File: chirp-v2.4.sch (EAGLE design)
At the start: 19 parts, among them IC1 TINY24/44/84-SSU, SW1 SPST_TACTFSMJSMA

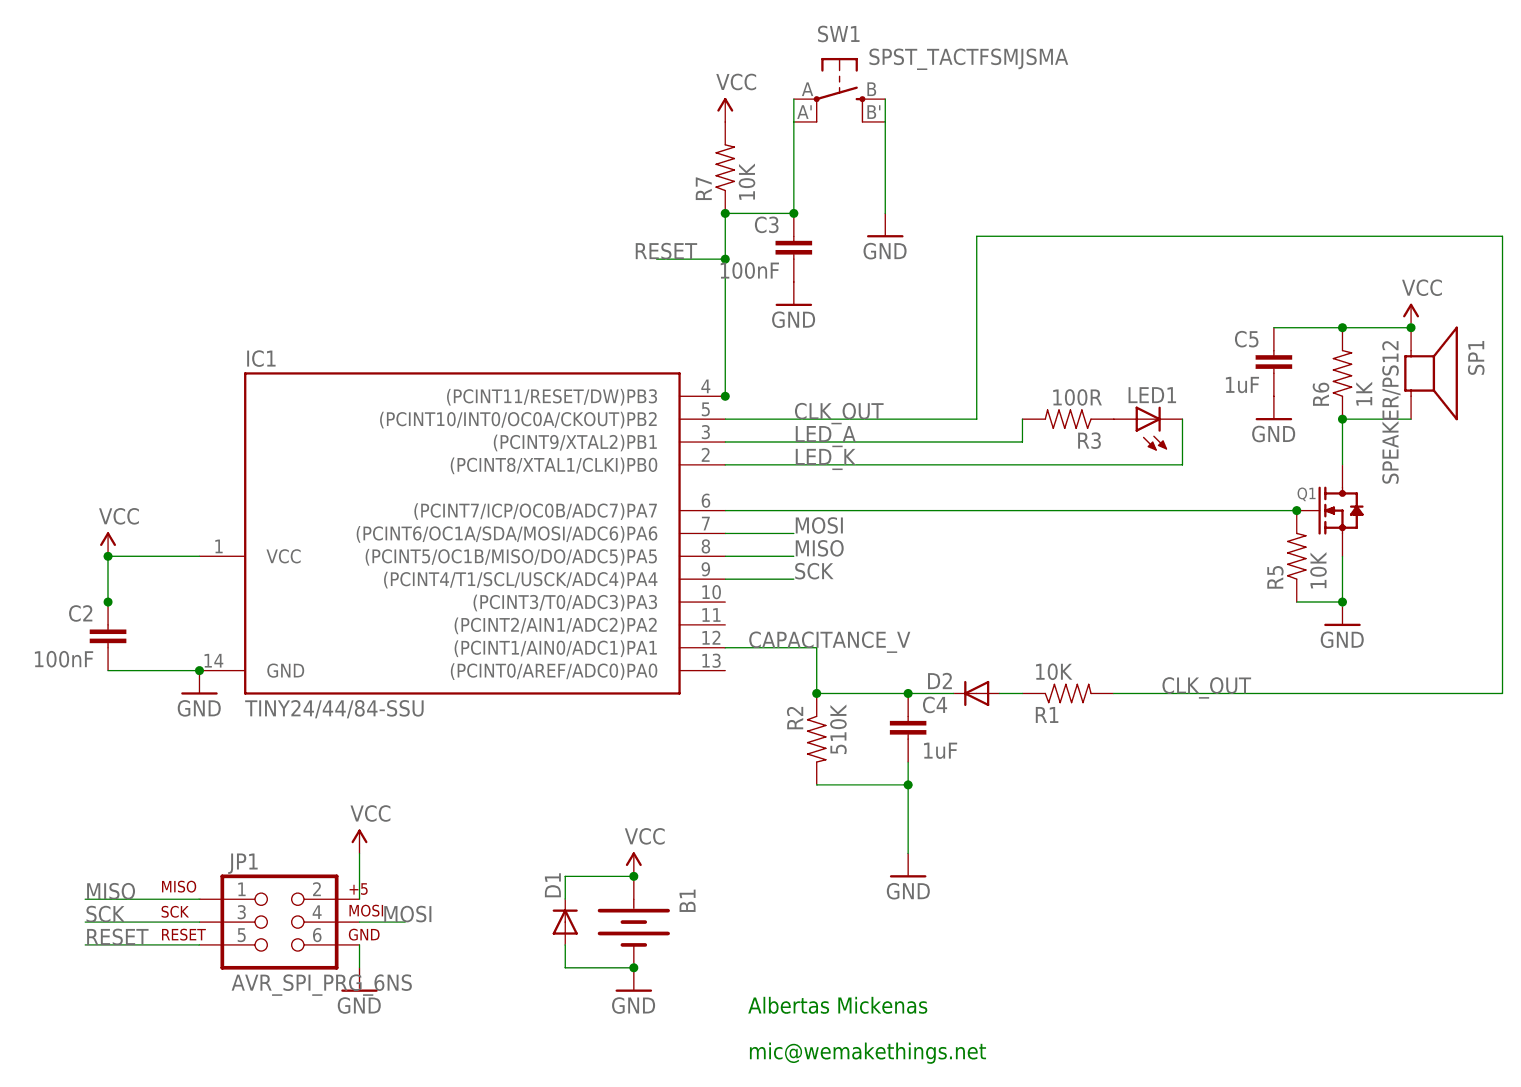
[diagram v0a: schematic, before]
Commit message: Silk changes
Removed Chirp labels
Added Watric labels
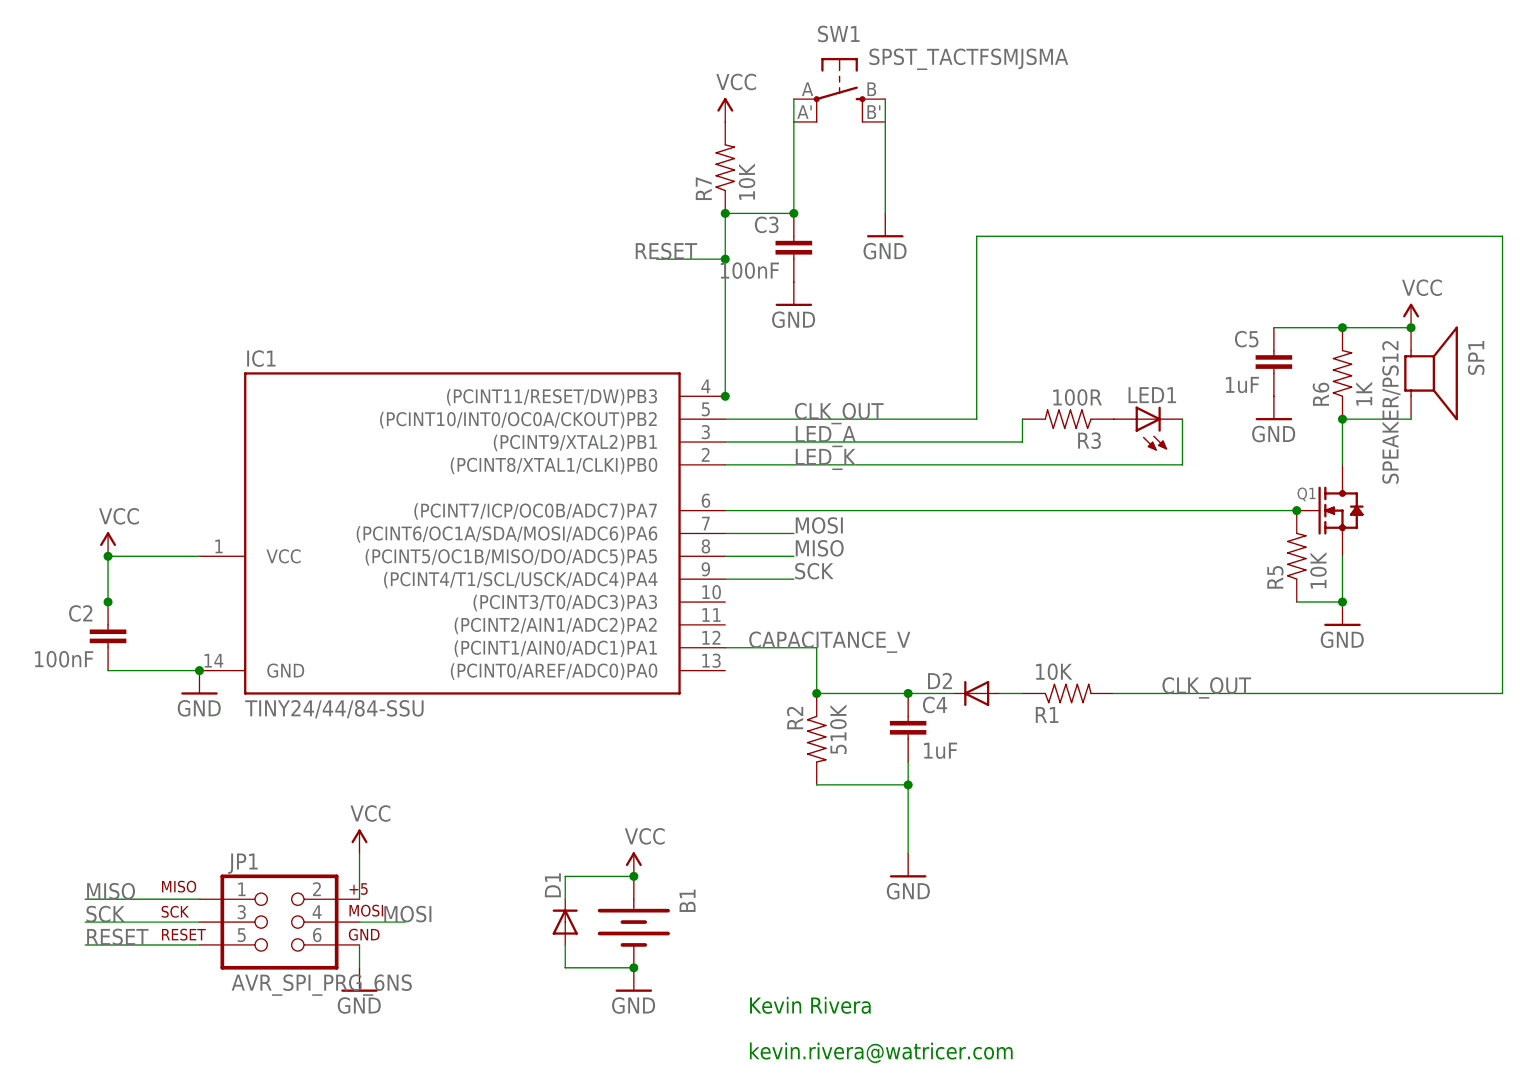
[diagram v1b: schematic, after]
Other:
- note added: "Kevin Rivera"
- note added: "kevin.rivera@watricer.com"
- note removed: "Albertas Mickenas"
- note removed: "mic@wemakethings.net"
